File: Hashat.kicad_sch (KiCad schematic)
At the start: 1 part, among them J1 Raspberry_Pi_2_3

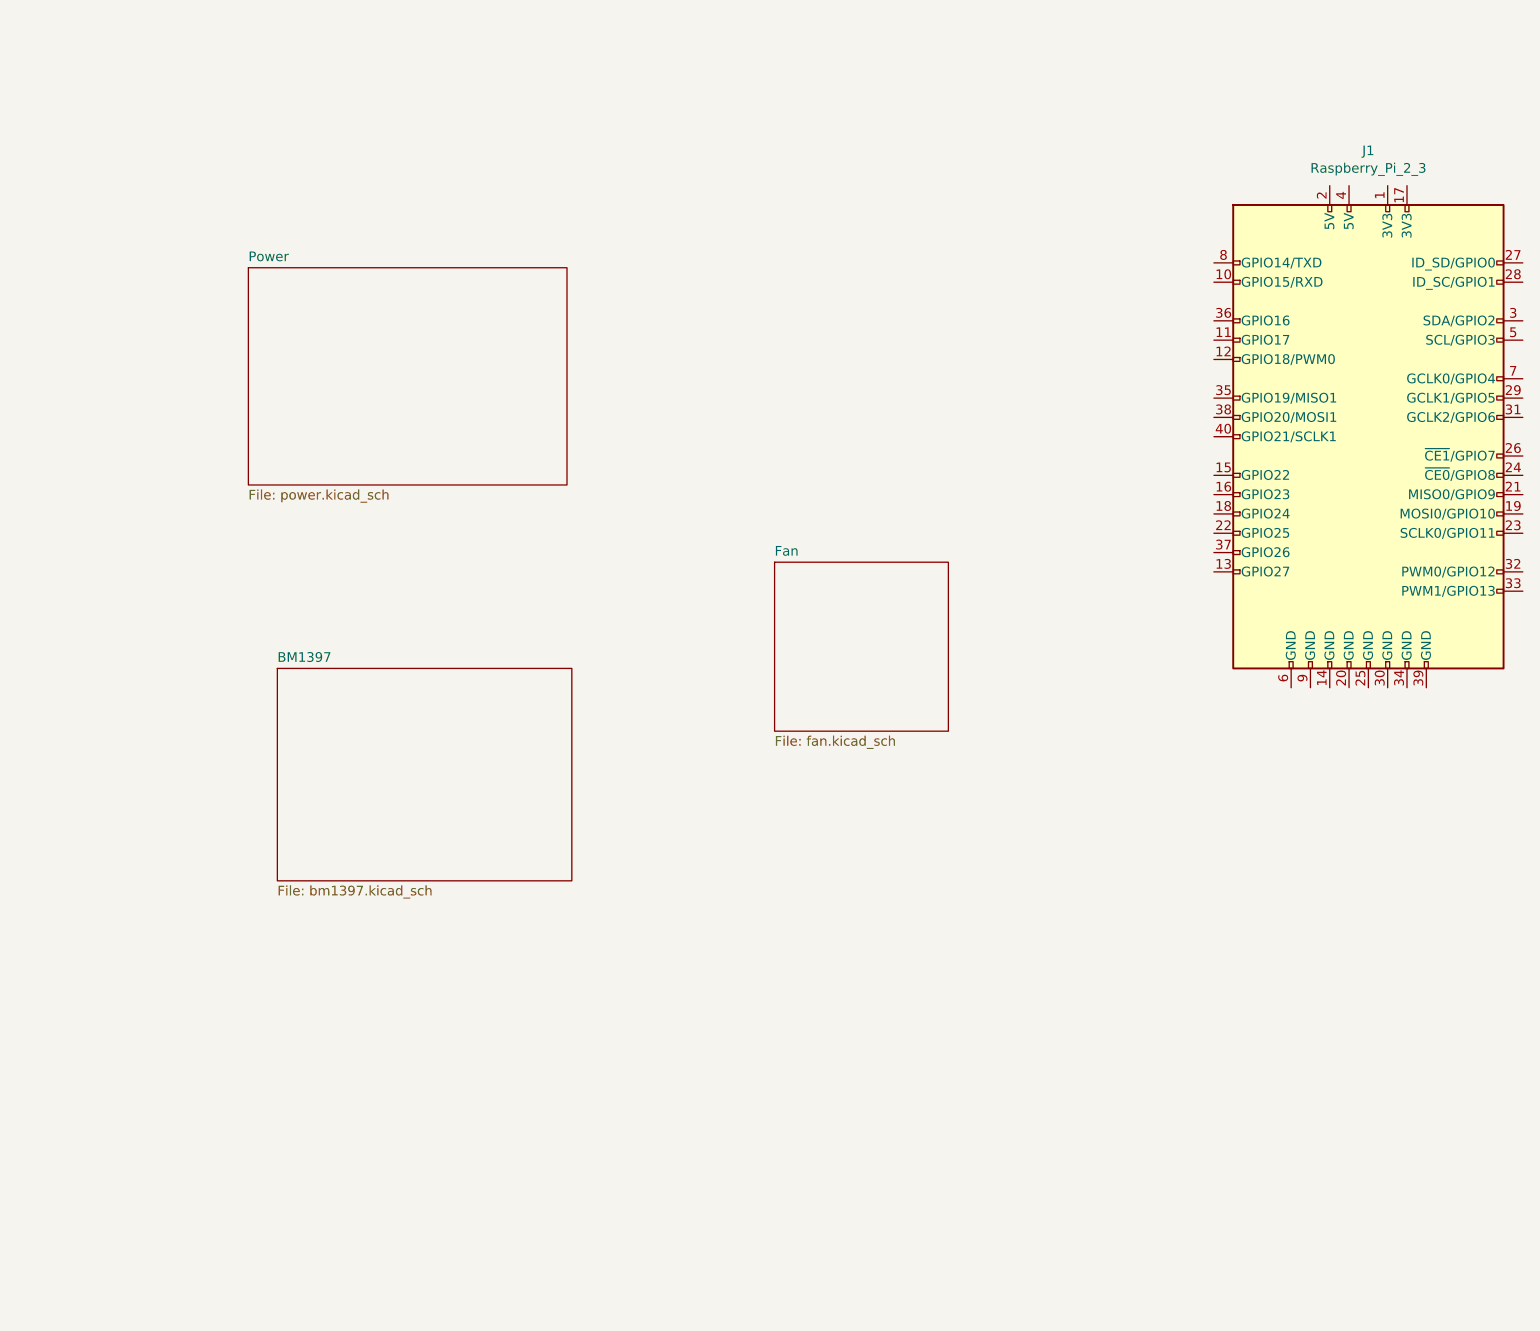
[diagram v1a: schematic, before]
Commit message: moved over a lot of schematic from the bitaxe
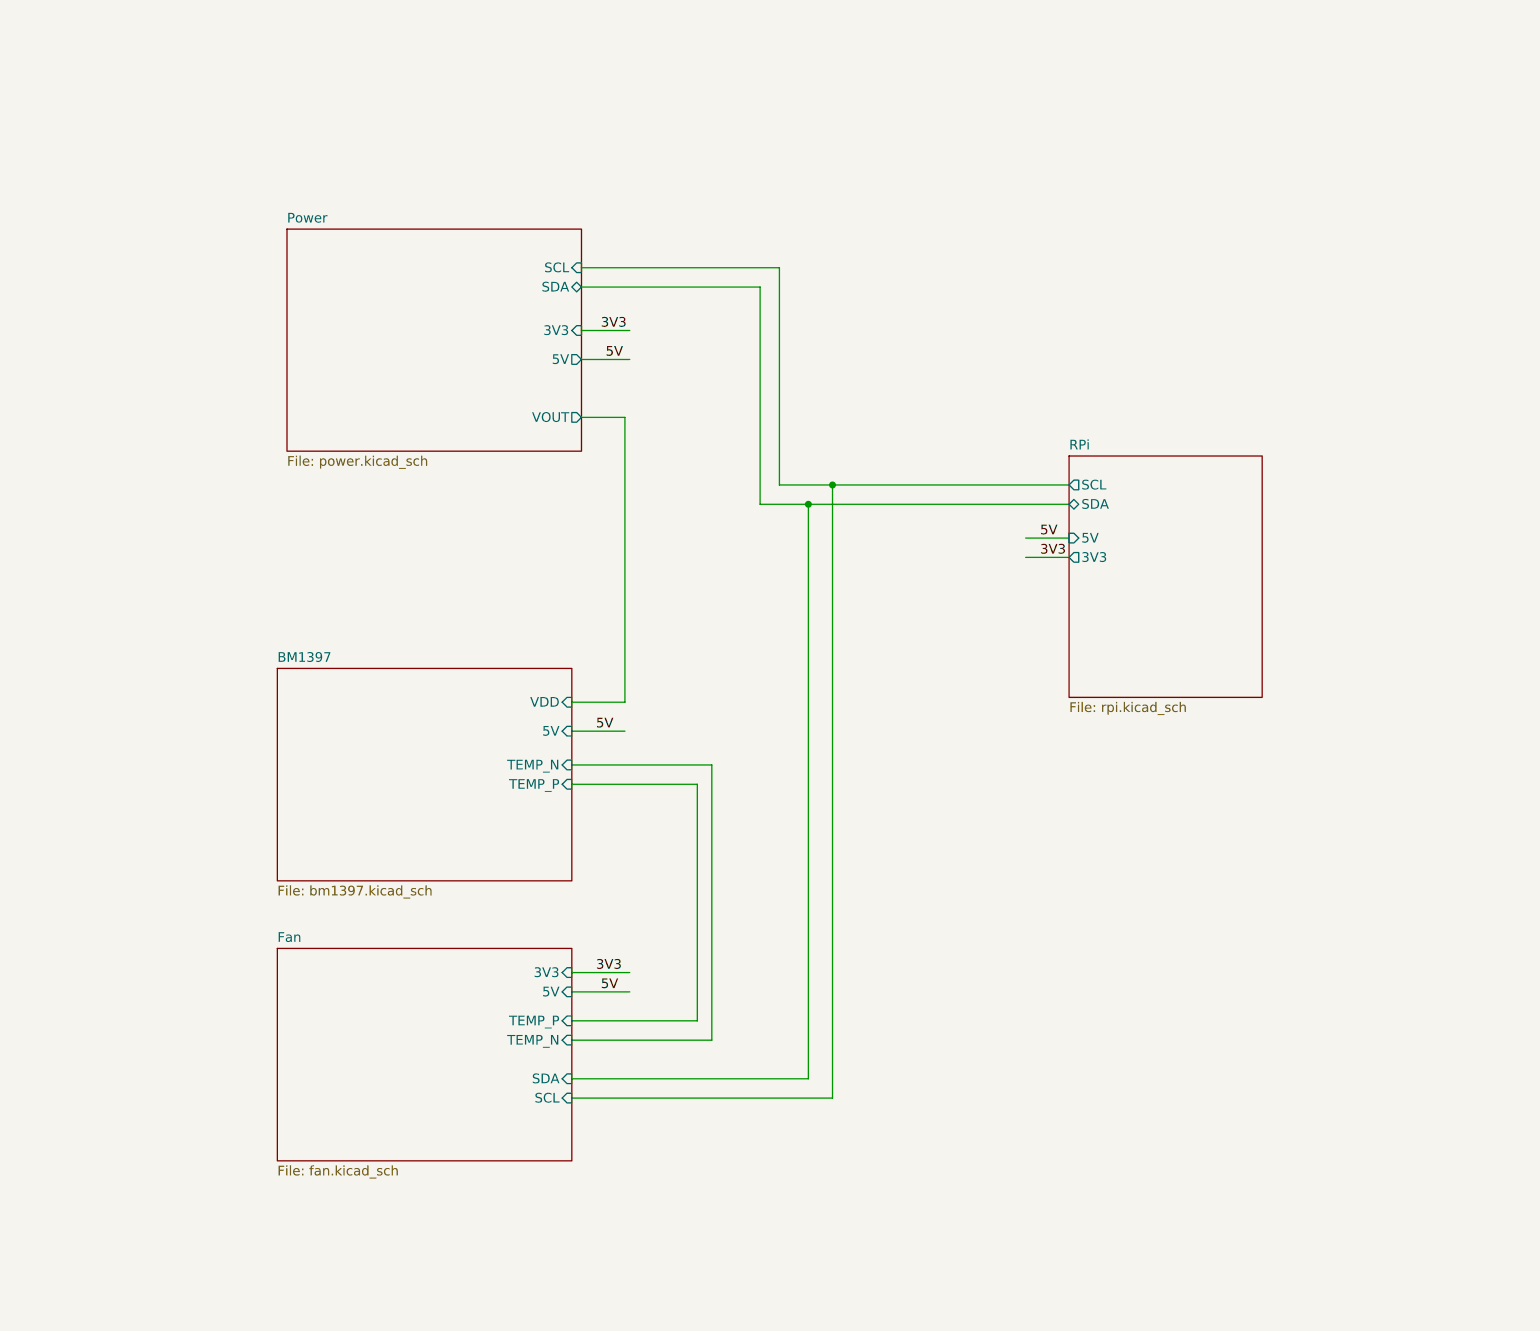
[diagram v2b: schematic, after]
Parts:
- removed J1: Raspberry_Pi_2_3, pihat:ESQ-120-14-T-D, symbol Connector:Raspberry_Pi_2_3
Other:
- added sheet RPi (rpi.kicad_sch)
- sheet BM1397 ports: added 5V, TEMP_N, TEMP_P, VDD; removed none
- sheet Fan ports: added 3V3, 5V, SCL, SDA, TEMP_N, TEMP_P; removed none
- sheet Power ports: added 3V3, 5V, SCL, SDA, VOUT; removed none
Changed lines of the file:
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@@
     (date "2023-04-21")
   )
-  (symbol (lib_id "Connector:Raspberry_Pi_2_3") (at 201.295 67.31 0) (unit 1)
-    (in_bom yes) (on_board yes) (dnp no)
-    (property "Reference" "J1" (at 201.295 29.6926 0)
-      (effects (font (size 1.27 1.27)))
-    )
-    (property "Value" "Raspberry_Pi_2_3" (at 201.295 32.004 0)
-      (effects (font (size 1.27 1.27)))
-    )
-    (property "Footprint" "pihat:ESQ-120-14-T-D" (at 201.295 67.31 0)
-      (effects (font (size 1.27 1.27)) hide)
-    )
-    (property "Datasheet" "https://www.raspberrypi.org/documentation/hardware/raspberrypi/schematics/rpi_SCH_3bplus_1p0_reduced.pdf" (at 201.295 67.31 0)
-      (effects (font (size 1.27 1.27)) hide)
-    )
-    (pin "1")
-    (pin "10")
-    (pin "11")
-    (pin "12")
-    (pin "13")
-    (pin "14")
-    (pin "15")
-    (pin "16")
-    (pin "17")
-    (pin "18")
-    (pin "19")
-    (pin "2")
-    (pin "20")
-    (pin "21")
-    (pin "22")
-    (pin "23")
-    (pin "24")
-    (pin "25")
-    (pin "26")
-    (pin "27")
-    (pin "28")
-    (pin "29")
-    (pin "3")
-    (pin "30")
-    (pin "31")
-    (pin "32")
-    (pin "33")
-    (pin "34")
-    (pin "35")
-    (pin "36")
-    (pin "37")
-    (pin "38")
-    (pin "39")
-    (pin "4")
-    (pin "40")
-    (pin "5")
-    (pin "6")
-    (pin "7")
-    (pin "8")
-    (pin "9")
+  (junction (at 130.81 73.66) (diameter 0) (color 0 0 0 0)
+  )
+  (junction (at 127.635 76.2) (diameter 0) (color 0 0 0 0)
+  )
+  (wire (pts (xy 97.79 53.34) (xy 104.14 53.34))
+    (stroke (width 0) (type default))
+  )
+  (wire (pts (xy 121.285 76.2) (xy 127.635 76.2))
+    (stroke (width 0) (type default))
+  )
+  (wire (pts (xy 97.79 64.77) (xy 103.505 64.77))
+    (stroke (width 0) (type default))
+  )
+  (wire (pts (xy 123.825 45.085) (xy 97.79 45.085))
+    (stroke (width 0) (type default))
+  )
+  (wire (pts (xy 97.79 47.625) (xy 121.285 47.625))
+    (stroke (width 0) (type default))
+  )
+  (wire (pts (xy 127.635 76.2) (xy 161.925 76.2))
+    (stroke (width 0) (type default))
+  )
+  (wire (pts (xy 96.52 144.145) (xy 113.03 144.145))
+    (stroke (width 0) (type default))
+  )
+  (wire (pts (xy 121.285 47.625) (xy 121.285 76.2))
+    (stroke (width 0) (type default))
+  )
+  (wire (pts (xy 156.21 80.645) (xy 161.925 80.645))
+    (stroke (width 0) (type default))
+  )
+  (wire (pts (xy 113.03 144.145) (xy 113.03 113.03))
+    (stroke (width 0) (type default))
+  )
+  (wire (pts (xy 156.21 83.185) (xy 161.925 83.185))
+    (stroke (width 0) (type default))
+  )
+  (wire (pts (xy 127.635 151.765) (xy 127.635 76.2))
+    (stroke (width 0) (type default))
+  )
+  (wire (pts (xy 96.52 151.765) (xy 127.635 151.765))
+    (stroke (width 0) (type default))
+  )
+  (wire (pts (xy 96.52 106.045) (xy 103.505 106.045))
+    (stroke (width 0) (type default))
+  )
+  (wire (pts (xy 113.03 113.03) (xy 96.52 113.03))
+    (stroke (width 0) (type default))
+  )
+  (wire (pts (xy 96.52 154.305) (xy 130.81 154.305))
+    (stroke (width 0) (type default))
+  )
+  (wire (pts (xy 114.935 110.49) (xy 114.935 146.685))
+    (stroke (width 0) (type default))
+  )
+  (wire (pts (xy 161.925 73.66) (xy 130.81 73.66))
+    (stroke (width 0) (type default))
+  )
+  (wire (pts (xy 97.79 57.15) (xy 104.14 57.15))
+    (stroke (width 0) (type default))
+  )
+  (wire (pts (xy 96.52 110.49) (xy 114.935 110.49))
+    (stroke (width 0) (type default))
+  )
+  (wire (pts (xy 130.81 73.66) (xy 123.825 73.66))
+    (stroke (width 0) (type default))
+  )
+  (wire (pts (xy 123.825 73.66) (xy 123.825 45.085))
+    (stroke (width 0) (type default))
+  )
+  (wire (pts (xy 114.935 146.685) (xy 96.52 146.685))
+    (stroke (width 0) (type default))
+  )
+  (wire (pts (xy 130.81 154.305) (xy 130.81 73.66))
+    (stroke (width 0) (type default))
+  )
+  (wire (pts (xy 103.505 64.77) (xy 103.505 102.235))
+    (stroke (width 0) (type default))
+  )
+  (wire (pts (xy 103.505 102.235) (xy 96.52 102.235))
+    (stroke (width 0) (type default))
+  )
+  (wire (pts (xy 96.52 137.795) (xy 104.14 137.795))
+    (stroke (width 0) (type default))
+  )
+  (wire (pts (xy 96.52 140.335) (xy 104.14 140.335))
+    (stroke (width 0) (type default))
+  )
+  (label "5V" (at 158.115 80.645 0) (fields_autoplaced)
+    (effects (font (size 1.27 1.27)) (justify left bottom))
+  )
+  (label "3V3" (at 100.33 53.34 0) (fields_autoplaced)
+    (effects (font (size 1.27 1.27)) (justify left bottom))
+  )
+  (label "5V" (at 100.33 140.335 0) (fields_autoplaced)
+    (effects (font (size 1.27 1.27)) (justify left bottom))
+  )
+  (label "5V" (at 99.695 106.045 0) (fields_autoplaced)
+    (effects (font (size 1.27 1.27)) (justify left bottom))
+  )
+  (label "3V3" (at 158.115 83.185 0) (fields_autoplaced)
+    (effects (font (size 1.27 1.27)) (justify left bottom))
+  )
+  (label "5V" (at 100.965 57.15 0) (fields_autoplaced)
+    (effects (font (size 1.27 1.27)) (justify left bottom))
+  )
+  (label "3V3" (at 99.695 137.795 0) (fields_autoplaced)
+    (effects (font (size 1.27 1.27)) (justify left bottom))
+  )
+  (sheet (at 161.925 69.85) (size 25.4 31.75) (fields_autoplaced)
+    (stroke (width 0.1524) (type solid))
+    (fill (color 255 255 194 1.0000))
+    (property "Sheetname" "RPi" (at 161.925 69.1384 0)
+      (effects (font (size 1.27 1.27)) (justify left bottom))
+    )
+    (property "Sheetfile" "rpi.kicad_sch" (at 161.925 102.1846 0)
+      (effects (font (size 1.27 1.27)) (justify left top))
+    )
+    (pin "SCL" output (at 161.925 73.66 180)
+      (effects (font (size 1.27 1.27)) (justify left))
+    )
+    (pin "SDA" bidirectional (at 161.925 76.2 180)
+      (effects (font (size 1.27 1.27)) (justify left))
+    )
+    (pin "5V" input (at 161.925 80.645 180)
+      (effects (font (size 1.27 1.27)) (justify left))
+    )
+    (pin "3V3" output (at 161.925 83.185 180)
+      (effects (font (size 1.27 1.27)) (justify left))
+    )
     (instances
       (project "Hashat"
-        (path "/00740941-7ad8-466a-a267-188591e2b5c4"
-          (reference "J1") (unit 1)
-        )
+        (path "/00740941-7ad8-466a-a267-188591e2b5c4" (page "5"))
       )
     )
@@
     (property "Sheetfile" "bm1397.kicad_sch" (at 57.785 126.3146 0)
       (effects (font (size 1.27 1.27)) (justify left top))
+    )
+    (pin "VDD" input (at 96.52 102.235 0)
+      (effects (font (size 1.27 1.27)) (justify right))
+    )
+    (pin "5V" input (at 96.52 106.045 0)
+      (effects (font (size 1.27 1.27)) (justify right))
+    )
+    (pin "TEMP_N" input (at 96.52 110.49 0)
+      (effects (font (size 1.27 1.27)) (justify right))
+    )
+    (pin "TEMP_P" input (at 96.52 113.03 0)
+      (effects (font (size 1.27 1.27)) (justify right))
     )
     (instances
@@
     )
   )
-  (sheet (at 53.975 45.085) (size 41.91 28.575) (fields_autoplaced)
-    (stroke (width 0.1524) (type solid))
-    (fill (color 255 255 194 1.0000))
-    (property "Sheetname" "Power" (at 53.975 44.3734 0)
-      (effects (font (size 1.27 1.27)) (justify left bottom))
-    )
-    (property "Sheetfile" "power.kicad_sch" (at 53.975 74.2446 0)
-      (effects (font (size 1.27 1.27)) (justify left top))
+  (sheet (at 59.055 40.005) (size 38.735 29.21) (fields_autoplaced)
+    (stroke (width 0.1524) (type solid))
+    (fill (color 255 255 194 1.0000))
+    (property "Sheetname" "Power" (at 59.055 39.2934 0)
+      (effects (font (size 1.27 1.27)) (justify left bottom))
+    )
+    (property "Sheetfile" "power.kicad_sch" (at 59.055 69.7996 0)
+      (effects (font (size 1.27 1.27)) (justify left top))
+    )
+    (pin "VOUT" output (at 97.79 64.77 0)
+      (effects (font (size 1.27 1.27)) (justify right))
+    )
+    (pin "SCL" input (at 97.79 45.085 0)
+      (effects (font (size 1.27 1.27)) (justify right))
+    )
+    (pin "SDA" bidirectional (at 97.79 47.625 0)
+      (effects (font (size 1.27 1.27)) (justify right))
+    )
+    (pin "3V3" input (at 97.79 53.34 0)
+      (effects (font (size 1.27 1.27)) (justify right))
+    )
+    (pin "5V" output (at 97.79 57.15 0)
+      (effects (font (size 1.27 1.27)) (justify right))
     )
     (instances
@@
     )
   )
-  (sheet (at 123.19 83.82) (size 22.86 22.225) (fields_autoplaced)
-    (stroke (width 0.1524) (type solid))
-    (fill (color 255 255 194 1.0000))
-    (property "Sheetname" "Fan" (at 123.19 83.1084 0)
-      (effects (font (size 1.27 1.27)) (justify left bottom))
-    )
-    (property "Sheetfile" "fan.kicad_sch" (at 123.19 106.6296 0)
-      (effects (font (size 1.27 1.27)) (justify left top))
-    )
-    (instances
+  (sheet (at 57.785 134.62) (size 38.735 27.94) (fields_autoplaced)
+    (stroke (width 0.1524) (type solid))
+    (fill (color 255 255 194 1.0000))
+    (property "Sheetname" "Fan" (at 57.785 133.9084 0)
+      (effects (font (size 1.27 1.27)) (justify left bottom))
+    )
+    (property "Sheetfile" "fan.kicad_sch" (at 57.785 163.1446 0)
+      (effects (font (size 1.27 1.27)) (justify left top))
+    )
+    (pin "5V" input (at 96.52 140.335 0)
+      (effects (font (size 1.27 1.27)) (justify right))
+    )
+    (pin "TEMP_P" input (at 96.52 144.145 0)
+      (effects (font (size 1.27 1.27)) (justify right))
+    )
+    (pin "TEMP_N" input (at 96.52 146.685 0)
+      (effects (font (size 1.27 1.27)) (justify right))
+    )
+    (pin "3V3" input (at 96.52 137.795 0)
+      (effects (font (size 1.27 1.27)) (justify right))
+    )
+    (pin "SDA" input (at 96.52 151.765 0)
+      (effects (font (size 1.27 1.27)) (justify right))
+    )
+    (pin "SCL" input (at 96.52 154.305 0)
+      (effects (font (size 1.27 1.27)) (justify right))
+    )
+    (instances
